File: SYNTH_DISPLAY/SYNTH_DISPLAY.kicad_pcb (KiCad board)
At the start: 2 copper layers, 51.9 x 64.3 mm, 27 parts, among them CON1 AVR-ISP-6, J1 Barrel_Jack, J2 Audio-Jack-3, J3 Conn_01x04, J4 Conn_01x01, J5 Conn_01x01, J6 Conn_01x01, J7 Conn_01x01, SW1 SW_Push_Dual, U1 L7805, U2 MSGEQ7, U3 ATTINY85-20PU

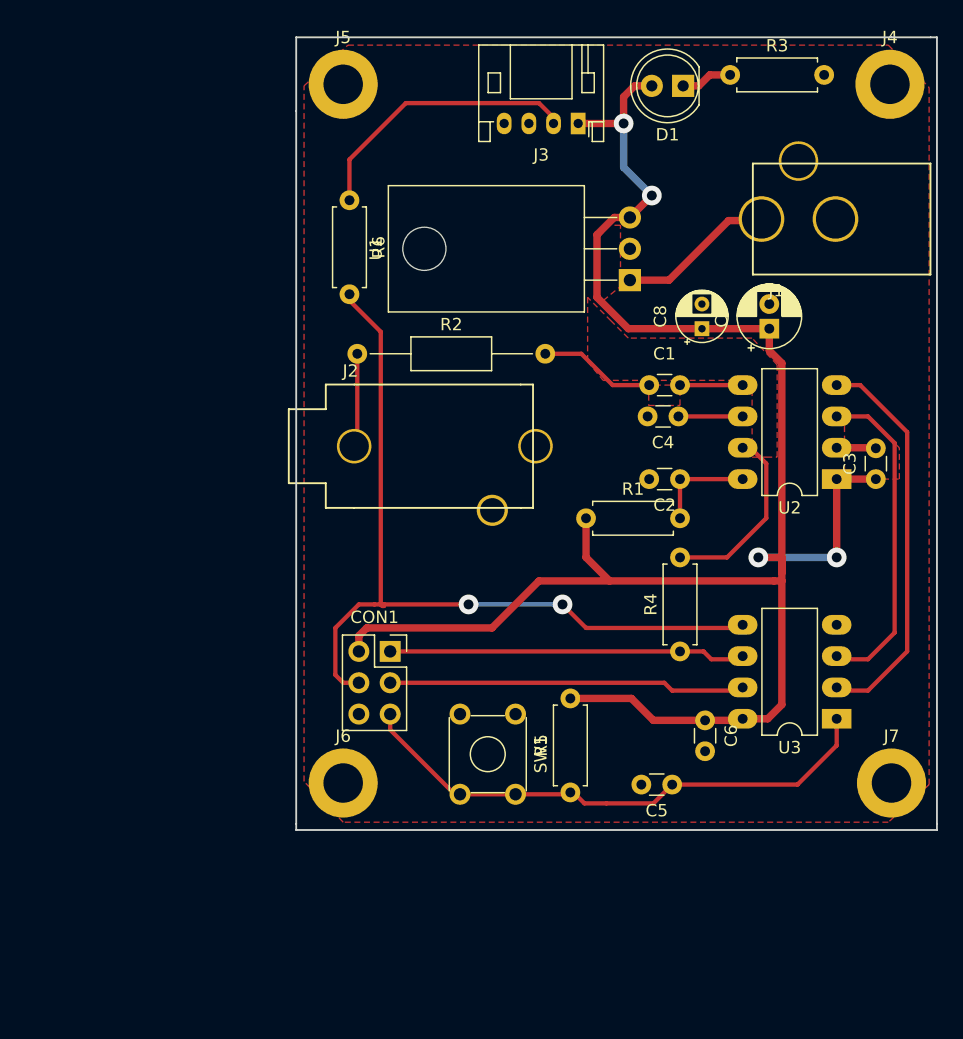
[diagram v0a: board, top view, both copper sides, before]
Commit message: changed from A4 to letter size sheet
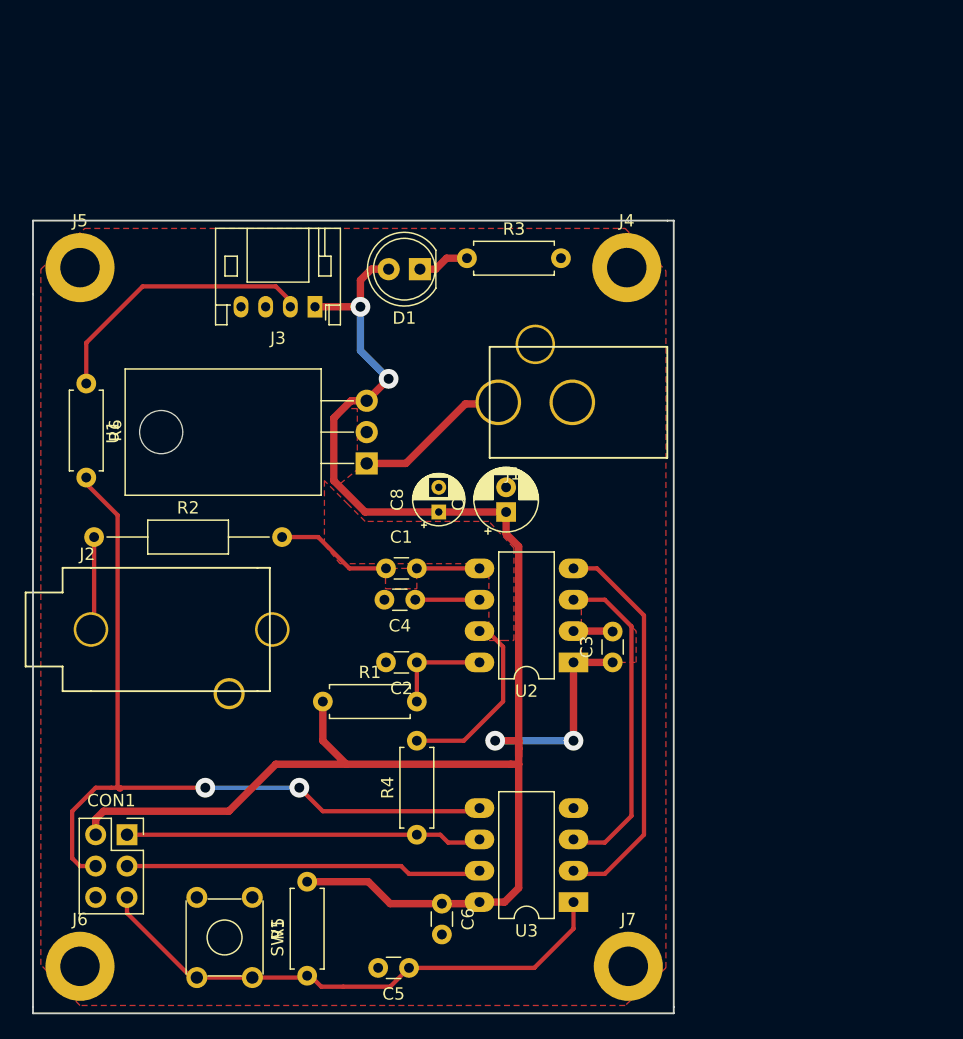
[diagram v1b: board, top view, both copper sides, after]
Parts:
- moved C1 26.0 mm to (150.7, 100.6)
- moved J2 26.0 mm to (124.3, 105.5)
- moved R1 26.0 mm to (143.1, 111.4)
- moved R4 26.0 mm to (150.7, 122.2)
- moved SW1 26.0 mm to (137.4, 127.3)
- moved C2 26.0 mm to (150.7, 108.2)
- moved C3 26.0 mm to (166.6, 108.2)
- moved C7 26.0 mm to (158.0, 96.0)
- moved C8 26.0 mm to (152.5, 96.0)
- moved D1 26.0 mm to (151.0, 76.3)
- moved J3 26.0 mm to (142.5, 79.4)
- moved J4 26.0 mm to (167.8, 76.2)
- moved R3 26.0 mm to (154.8, 75.4)
- moved R6 26.0 mm to (124.0, 85.6)
- moved CON1 26.0 mm to (127.3, 122.2)
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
